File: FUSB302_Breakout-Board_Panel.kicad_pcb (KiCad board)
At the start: 2 copper layers, 100 x 100 mm, 75 parts, among them J1 Conn_01x07_Male, J2 Conn_01x07_Male, U1 FUSB302BMPX

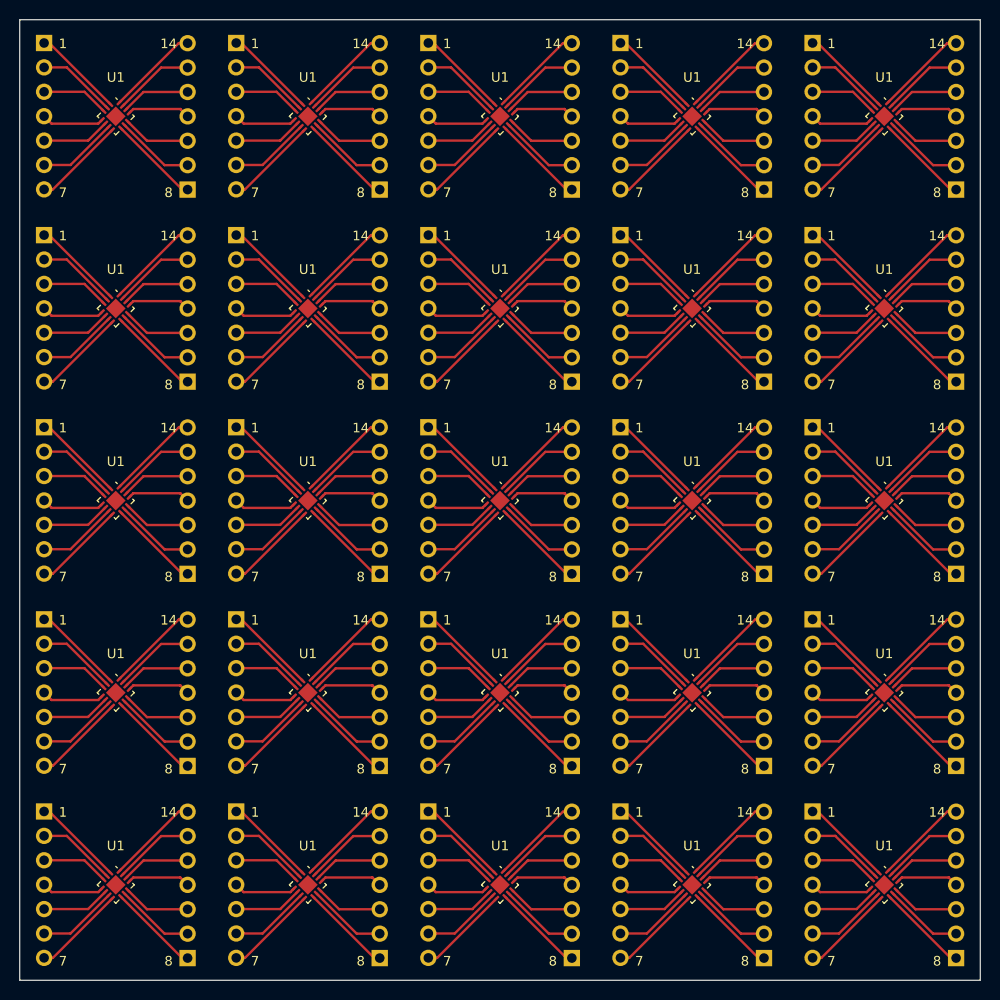
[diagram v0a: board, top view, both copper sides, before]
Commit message: Mod: PCB, added vias to filled zone on the bottom for a better heat path Mod: Panel, with new pcb Mod: Exports
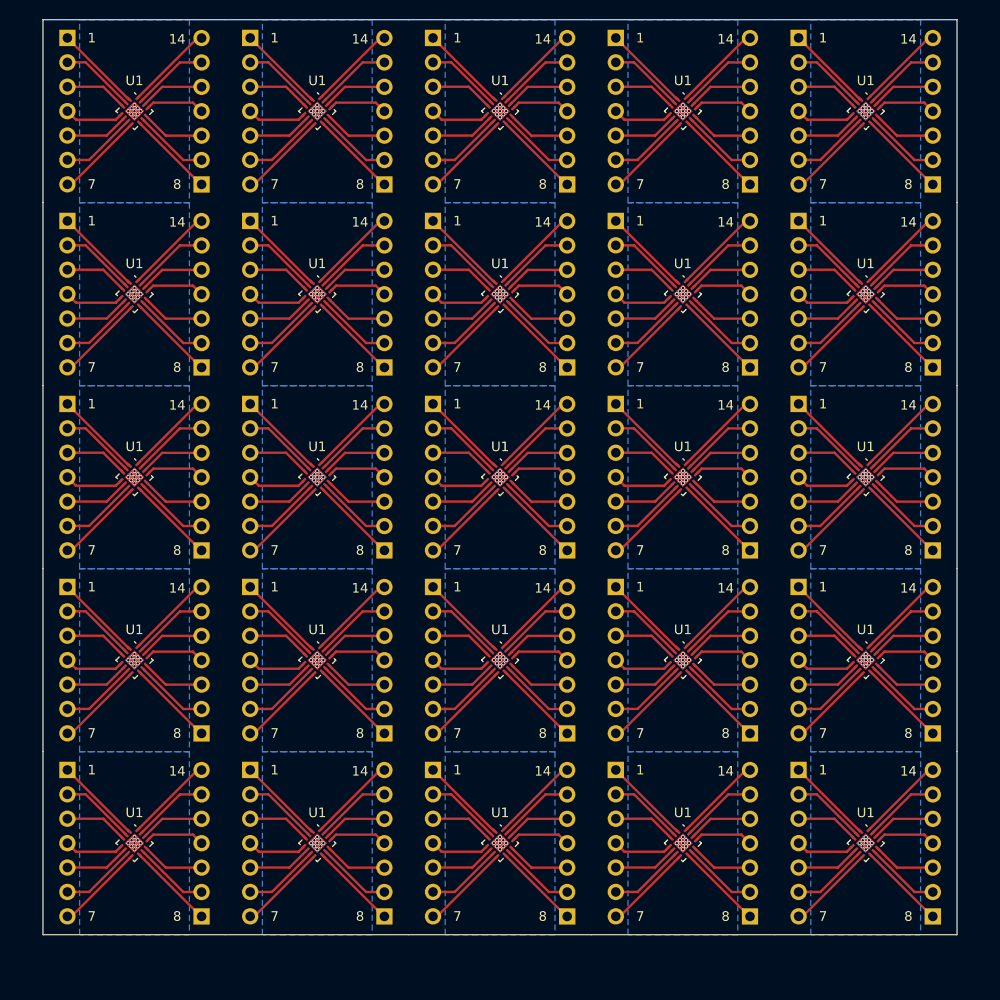
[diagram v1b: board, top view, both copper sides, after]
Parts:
- removed the J1 at (141.0, 92.4)
- removed the J1 at (101.0, 72.4)
- removed the J1 at (121.0, 72.4)
- removed the J1 at (121.0, 132.4)
- removed the J1 at (101.0, 112.4)
- removed the J1 at (141.0, 132.4)
- removed the J1 at (181.0, 92.4)
- removed the J1 at (181.0, 112.4)
- removed the J1 at (121.0, 92.4)
- removed the J1 at (141.0, 72.4)
- removed the J1 at (101.0, 132.4)
- removed the J1 at (181.0, 52.4)
- removed the J1 at (161.0, 92.4)
- removed the J1 at (181.0, 72.4)
- removed the J1 at (101.0, 92.4)
- removed the J1 at (181.0, 132.4)
- removed the J1 at (141.0, 52.4)
- removed the J1 at (161.0, 112.4)
- removed the J1 at (141.0, 112.4)
- removed the J1 at (121.0, 52.4)
- removed the J1 at (101.0, 52.4)
- removed the J1 at (121.0, 112.4)
- removed the J1 at (161.0, 72.4)
- removed the J1 at (161.0, 132.4)
- removed the J1 at (161.0, 52.4)
- removed the J2 at (156.0, 147.7)
- removed the J2 at (176.0, 107.7)
- removed the J2 at (116.0, 147.7)
- removed the J2 at (176.0, 67.7)
- removed the J2 at (116.0, 87.7)
- removed the J2 at (176.0, 87.7)
- removed the J2 at (136.0, 107.7)
- removed the J2 at (116.0, 127.7)
- removed the J2 at (196.0, 87.7)
- removed the J2 at (196.0, 147.7)
- removed the J2 at (136.0, 147.7)
- removed the J2 at (196.0, 127.7)
- removed the J2 at (176.0, 147.7)
- removed the J2 at (116.0, 107.7)
- removed the J2 at (196.0, 107.7)
- removed the J2 at (136.0, 87.7)
- removed the J2 at (196.0, 67.7)
- removed the J2 at (156.0, 127.7)
- removed the J2 at (136.0, 127.7)
- removed the J2 at (136.0, 67.7)
- removed the J2 at (116.0, 67.7)
- removed the J2 at (156.0, 67.7)
- removed the J2 at (176.0, 127.7)
- removed the J2 at (156.0, 87.7)
- removed the J2 at (156.0, 107.7)
- removed the U1 at (168.5, 120.1)
- removed the U1 at (168.5, 100.1)
- removed the U1 at (148.5, 100.1)
- removed the U1 at (168.5, 60.1)
- removed the U1 at (128.5, 120.1)
- removed the U1 at (108.5, 120.1)
- removed the U1 at (148.5, 80.1)
- removed the U1 at (188.5, 140.1)
- removed the U1 at (108.5, 100.1)
- removed the U1 at (188.5, 120.1)
- removed the U1 at (128.5, 140.1)
- removed the U1 at (108.5, 80.1)
- removed the U1 at (128.5, 60.1)
- removed the U1 at (108.5, 140.1)
- removed the U1 at (188.5, 60.1)
- removed the U1 at (168.5, 80.1)
- removed the U1 at (168.5, 140.1)
- removed the U1 at (148.5, 140.1)
- removed the U1 at (128.5, 80.1)
- removed the U1 at (148.5, 60.1)
- removed the U1 at (148.5, 120.1)
- removed the U1 at (128.5, 100.1)
- removed the U1 at (108.5, 60.1)
- removed the U1 at (188.5, 80.1)
- removed the U1 at (188.5, 100.1)
- added J1: Conn_01x07_Male, Connector_PinHeader_2.54mm:PinHeader_1x07_P2.54mm_Vertical, B.Cu at (160.6, 128.1)
- added J1: Conn_01x07_Male, Connector_PinHeader_2.54mm:PinHeader_1x07_P2.54mm_Vertical, B.Cu at (179.6, 51.9)
- added J1: Conn_01x07_Male, Connector_PinHeader_2.54mm:PinHeader_1x07_P2.54mm_Vertical, B.Cu at (141.5, 71.0)
- added J1: Conn_01x07_Male, Connector_PinHeader_2.54mm:PinHeader_1x07_P2.54mm_Vertical, B.Cu at (179.6, 109.0)
- added J1: Conn_01x07_Male, Connector_PinHeader_2.54mm:PinHeader_1x07_P2.54mm_Vertical, B.Cu at (103.5, 109.0)
- added J1: Conn_01x07_Male, Connector_PinHeader_2.54mm:PinHeader_1x07_P2.54mm_Vertical, B.Cu at (160.6, 71.0)
- added J1: Conn_01x07_Male, Connector_PinHeader_2.54mm:PinHeader_1x07_P2.54mm_Vertical, B.Cu at (103.5, 71.0)
- added J1: Conn_01x07_Male, Connector_PinHeader_2.54mm:PinHeader_1x07_P2.54mm_Vertical, B.Cu at (103.5, 90.0)
- added J1: Conn_01x07_Male, Connector_PinHeader_2.54mm:PinHeader_1x07_P2.54mm_Vertical, B.Cu at (179.6, 71.0)
- added J1: Conn_01x07_Male, Connector_PinHeader_2.54mm:PinHeader_1x07_P2.54mm_Vertical, B.Cu at (122.5, 109.0)
- added J1: Conn_01x07_Male, Connector_PinHeader_2.54mm:PinHeader_1x07_P2.54mm_Vertical, B.Cu at (179.6, 128.1)
- added J1: Conn_01x07_Male, Connector_PinHeader_2.54mm:PinHeader_1x07_P2.54mm_Vertical, B.Cu at (103.5, 51.9)
- added J1: Conn_01x07_Male, Connector_PinHeader_2.54mm:PinHeader_1x07_P2.54mm_Vertical, B.Cu at (160.6, 109.0)
- added J1: Conn_01x07_Male, Connector_PinHeader_2.54mm:PinHeader_1x07_P2.54mm_Vertical, B.Cu at (141.5, 109.0)
- added J1: Conn_01x07_Male, Connector_PinHeader_2.54mm:PinHeader_1x07_P2.54mm_Vertical, B.Cu at (141.5, 51.9)
- added J1: Conn_01x07_Male, Connector_PinHeader_2.54mm:PinHeader_1x07_P2.54mm_Vertical, B.Cu at (141.5, 90.0)
- added J1: Conn_01x07_Male, Connector_PinHeader_2.54mm:PinHeader_1x07_P2.54mm_Vertical, B.Cu at (122.5, 128.1)
- added J1: Conn_01x07_Male, Connector_PinHeader_2.54mm:PinHeader_1x07_P2.54mm_Vertical, B.Cu at (122.5, 71.0)
- added J1: Conn_01x07_Male, Connector_PinHeader_2.54mm:PinHeader_1x07_P2.54mm_Vertical, B.Cu at (179.6, 90.0)
- added J1: Conn_01x07_Male, Connector_PinHeader_2.54mm:PinHeader_1x07_P2.54mm_Vertical, B.Cu at (160.6, 90.0)
- added J1: Conn_01x07_Male, Connector_PinHeader_2.54mm:PinHeader_1x07_P2.54mm_Vertical, B.Cu at (141.5, 128.1)
- added J1: Conn_01x07_Male, Connector_PinHeader_2.54mm:PinHeader_1x07_P2.54mm_Vertical, B.Cu at (122.5, 51.9)
- added J1: Conn_01x07_Male, Connector_PinHeader_2.54mm:PinHeader_1x07_P2.54mm_Vertical, B.Cu at (160.6, 51.9)
- added J1: Conn_01x07_Male, Connector_PinHeader_2.54mm:PinHeader_1x07_P2.54mm_Vertical, B.Cu at (103.5, 128.1)
- added J1: Conn_01x07_Male, Connector_PinHeader_2.54mm:PinHeader_1x07_P2.54mm_Vertical, B.Cu at (122.5, 90.0)
- added J2: Conn_01x07_Male, Connector_PinHeader_2.54mm:PinHeader_1x07_P2.54mm_Vertical, B.Cu at (193.6, 124.3)
- added J2: Conn_01x07_Male, Connector_PinHeader_2.54mm:PinHeader_1x07_P2.54mm_Vertical, B.Cu at (155.5, 143.3)
- added J2: Conn_01x07_Male, Connector_PinHeader_2.54mm:PinHeader_1x07_P2.54mm_Vertical, B.Cu at (155.5, 124.3)
- added J2: Conn_01x07_Male, Connector_PinHeader_2.54mm:PinHeader_1x07_P2.54mm_Vertical, B.Cu at (136.5, 105.2)
- added J2: Conn_01x07_Male, Connector_PinHeader_2.54mm:PinHeader_1x07_P2.54mm_Vertical, B.Cu at (136.5, 124.3)
- added J2: Conn_01x07_Male, Connector_PinHeader_2.54mm:PinHeader_1x07_P2.54mm_Vertical, B.Cu at (155.5, 105.2)
- added J2: Conn_01x07_Male, Connector_PinHeader_2.54mm:PinHeader_1x07_P2.54mm_Vertical, B.Cu at (193.6, 105.2)
- added J2: Conn_01x07_Male, Connector_PinHeader_2.54mm:PinHeader_1x07_P2.54mm_Vertical, B.Cu at (193.6, 143.3)
- added J2: Conn_01x07_Male, Connector_PinHeader_2.54mm:PinHeader_1x07_P2.54mm_Vertical, B.Cu at (136.5, 143.3)
- added J2: Conn_01x07_Male, Connector_PinHeader_2.54mm:PinHeader_1x07_P2.54mm_Vertical, B.Cu at (174.5, 67.2)
- added J2: Conn_01x07_Male, Connector_PinHeader_2.54mm:PinHeader_1x07_P2.54mm_Vertical, B.Cu at (117.4, 105.2)
- added J2: Conn_01x07_Male, Connector_PinHeader_2.54mm:PinHeader_1x07_P2.54mm_Vertical, B.Cu at (174.5, 143.3)
- added J2: Conn_01x07_Male, Connector_PinHeader_2.54mm:PinHeader_1x07_P2.54mm_Vertical, B.Cu at (117.4, 124.3)
- added J2: Conn_01x07_Male, Connector_PinHeader_2.54mm:PinHeader_1x07_P2.54mm_Vertical, B.Cu at (117.4, 67.2)
- added J2: Conn_01x07_Male, Connector_PinHeader_2.54mm:PinHeader_1x07_P2.54mm_Vertical, B.Cu at (174.5, 86.2)
- added J2: Conn_01x07_Male, Connector_PinHeader_2.54mm:PinHeader_1x07_P2.54mm_Vertical, B.Cu at (117.4, 143.3)
- added J2: Conn_01x07_Male, Connector_PinHeader_2.54mm:PinHeader_1x07_P2.54mm_Vertical, B.Cu at (174.5, 124.3)
- added J2: Conn_01x07_Male, Connector_PinHeader_2.54mm:PinHeader_1x07_P2.54mm_Vertical, B.Cu at (155.5, 86.2)
- added J2: Conn_01x07_Male, Connector_PinHeader_2.54mm:PinHeader_1x07_P2.54mm_Vertical, B.Cu at (136.5, 67.2)
- added J2: Conn_01x07_Male, Connector_PinHeader_2.54mm:PinHeader_1x07_P2.54mm_Vertical, B.Cu at (193.6, 86.2)
- added J2: Conn_01x07_Male, Connector_PinHeader_2.54mm:PinHeader_1x07_P2.54mm_Vertical, B.Cu at (174.5, 105.2)
- added J2: Conn_01x07_Male, Connector_PinHeader_2.54mm:PinHeader_1x07_P2.54mm_Vertical, B.Cu at (193.6, 67.2)
- added J2: Conn_01x07_Male, Connector_PinHeader_2.54mm:PinHeader_1x07_P2.54mm_Vertical, B.Cu at (117.4, 86.2)
- added J2: Conn_01x07_Male, Connector_PinHeader_2.54mm:PinHeader_1x07_P2.54mm_Vertical, B.Cu at (136.5, 86.2)
- added J2: Conn_01x07_Male, Connector_PinHeader_2.54mm:PinHeader_1x07_P2.54mm_Vertical, B.Cu at (155.5, 67.2)
- added U1: FUSB302BMPX, Package_DFN_QFN:WQFN-14-1EP_2.5x2.5mm_P0.5mm_EP1.45x1.45mm, F.Cu at (110.5, 78.6)
- added U1: FUSB302BMPX, Package_DFN_QFN:WQFN-14-1EP_2.5x2.5mm_P0.5mm_EP1.45x1.45mm, F.Cu at (148.5, 116.7)
- added U1: FUSB302BMPX, Package_DFN_QFN:WQFN-14-1EP_2.5x2.5mm_P0.5mm_EP1.45x1.45mm, F.Cu at (110.5, 59.5)
- added U1: FUSB302BMPX, Package_DFN_QFN:WQFN-14-1EP_2.5x2.5mm_P0.5mm_EP1.45x1.45mm, F.Cu at (167.5, 78.6)
- added U1: FUSB302BMPX, Package_DFN_QFN:WQFN-14-1EP_2.5x2.5mm_P0.5mm_EP1.45x1.45mm, F.Cu at (167.5, 59.5)
- added U1: FUSB302BMPX, Package_DFN_QFN:WQFN-14-1EP_2.5x2.5mm_P0.5mm_EP1.45x1.45mm, F.Cu at (186.6, 116.7)
- added U1: FUSB302BMPX, Package_DFN_QFN:WQFN-14-1EP_2.5x2.5mm_P0.5mm_EP1.45x1.45mm, F.Cu at (148.5, 135.7)
- added U1: FUSB302BMPX, Package_DFN_QFN:WQFN-14-1EP_2.5x2.5mm_P0.5mm_EP1.45x1.45mm, F.Cu at (167.5, 97.6)
- added U1: FUSB302BMPX, Package_DFN_QFN:WQFN-14-1EP_2.5x2.5mm_P0.5mm_EP1.45x1.45mm, F.Cu at (186.6, 78.6)
- added U1: FUSB302BMPX, Package_DFN_QFN:WQFN-14-1EP_2.5x2.5mm_P0.5mm_EP1.45x1.45mm, F.Cu at (129.5, 59.5)
- added U1: FUSB302BMPX, Package_DFN_QFN:WQFN-14-1EP_2.5x2.5mm_P0.5mm_EP1.45x1.45mm, F.Cu at (129.5, 78.6)
- added U1: FUSB302BMPX, Package_DFN_QFN:WQFN-14-1EP_2.5x2.5mm_P0.5mm_EP1.45x1.45mm, F.Cu at (148.5, 59.5)
- added U1: FUSB302BMPX, Package_DFN_QFN:WQFN-14-1EP_2.5x2.5mm_P0.5mm_EP1.45x1.45mm, F.Cu at (186.6, 59.5)
- added U1: FUSB302BMPX, Package_DFN_QFN:WQFN-14-1EP_2.5x2.5mm_P0.5mm_EP1.45x1.45mm, F.Cu at (167.5, 116.7)
- added U1: FUSB302BMPX, Package_DFN_QFN:WQFN-14-1EP_2.5x2.5mm_P0.5mm_EP1.45x1.45mm, F.Cu at (167.5, 135.7)
- added U1: FUSB302BMPX, Package_DFN_QFN:WQFN-14-1EP_2.5x2.5mm_P0.5mm_EP1.45x1.45mm, F.Cu at (110.5, 116.7)
- added U1: FUSB302BMPX, Package_DFN_QFN:WQFN-14-1EP_2.5x2.5mm_P0.5mm_EP1.45x1.45mm, F.Cu at (186.6, 135.7)
- added U1: FUSB302BMPX, Package_DFN_QFN:WQFN-14-1EP_2.5x2.5mm_P0.5mm_EP1.45x1.45mm, F.Cu at (110.5, 135.7)
- added U1: FUSB302BMPX, Package_DFN_QFN:WQFN-14-1EP_2.5x2.5mm_P0.5mm_EP1.45x1.45mm, F.Cu at (148.5, 78.6)
- added U1: FUSB302BMPX, Package_DFN_QFN:WQFN-14-1EP_2.5x2.5mm_P0.5mm_EP1.45x1.45mm, F.Cu at (110.5, 97.6)
- added U1: FUSB302BMPX, Package_DFN_QFN:WQFN-14-1EP_2.5x2.5mm_P0.5mm_EP1.45x1.45mm, F.Cu at (148.5, 97.6)
- added U1: FUSB302BMPX, Package_DFN_QFN:WQFN-14-1EP_2.5x2.5mm_P0.5mm_EP1.45x1.45mm, F.Cu at (186.6, 97.6)
- added U1: FUSB302BMPX, Package_DFN_QFN:WQFN-14-1EP_2.5x2.5mm_P0.5mm_EP1.45x1.45mm, F.Cu at (129.5, 97.6)
- added U1: FUSB302BMPX, Package_DFN_QFN:WQFN-14-1EP_2.5x2.5mm_P0.5mm_EP1.45x1.45mm, F.Cu at (129.5, 135.7)
- added U1: FUSB302BMPX, Package_DFN_QFN:WQFN-14-1EP_2.5x2.5mm_P0.5mm_EP1.45x1.45mm, F.Cu at (129.5, 116.7)
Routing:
- net Board_0-VCONN: track 15.6 -> 14.6 mm
- net Board_5-VCONN: track 15.6 -> 14.6 mm
- net Board_20-VCONN: track 15.6 -> 14.6 mm
- net Board_19-GND: track 17.9 -> 16.9 mm, vias 0 -> 9
- net Board_18-GND: track 17.9 -> 16.9 mm, vias 0 -> 9
- net Board_17-GND: track 17.9 -> 16.9 mm, vias 0 -> 9
- net Board_16-GND: track 17.9 -> 16.9 mm, vias 0 -> 9
- net Board_14-GND: track 17.9 -> 16.9 mm, vias 0 -> 9
- net Board_13-GND: track 17.9 -> 16.9 mm, vias 0 -> 9
- net Board_12-GND: track 17.9 -> 16.9 mm, vias 0 -> 9
- net Board_11-GND: track 17.9 -> 16.9 mm, vias 0 -> 9
- net Board_9-GND: track 17.9 -> 16.9 mm, vias 0 -> 9
- net Board_8-GND: track 17.9 -> 16.9 mm, vias 0 -> 9
- net Board_7-GND: track 17.9 -> 16.9 mm, vias 0 -> 9
- net Board_6-GND: track 17.9 -> 16.9 mm, vias 0 -> 9
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- added copper zone on B.Cu, net Board_0-GND
- added copper zone on B.Cu, net Board_1-GND
- added copper zone on B.Cu, net Board_10-GND
- added copper zone on B.Cu, net Board_11-GND
- added copper zone on B.Cu, net Board_12-GND
- added copper zone on B.Cu, net Board_13-GND
- added copper zone on B.Cu, net Board_14-GND
- added copper zone on B.Cu, net Board_15-GND
- added copper zone on B.Cu, net Board_16-GND
- added copper zone on B.Cu, net Board_17-GND
- added copper zone on B.Cu, net Board_18-GND
- added copper zone on B.Cu, net Board_19-GND
- added copper zone on B.Cu, net Board_2-GND
- added copper zone on B.Cu, net Board_20-GND
- added copper zone on B.Cu, net Board_21-GND
- added copper zone on B.Cu, net Board_22-GND
- added copper zone on B.Cu, net Board_23-GND
- added copper zone on B.Cu, net Board_24-GND
- added copper zone on B.Cu, net Board_3-GND
- added copper zone on B.Cu, net Board_4-GND
- added copper zone on B.Cu, net Board_5-GND
- added copper zone on B.Cu, net Board_6-GND
- added copper zone on B.Cu, net Board_7-GND
- added copper zone on B.Cu, net Board_8-GND
- added copper zone on B.Cu, net Board_9-GND
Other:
- board size 100 x 100 mm -> 95.1 x 95.2 mm

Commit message: Mod: Bottom solder mask, pasted logo in to it and exported the pcb with the v-cuts
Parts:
- added G***: LOGO, drawings:elektronik-emblem_3x3.5_solder, B.Cu at (186.6, 130.0)
- added G***: LOGO, drawings:elektronik-emblem_3x3.5_solder, B.Cu at (110.5, 53.8)
- added G***: LOGO, drawings:elektronik-emblem_3x3.5_solder, B.Cu at (186.6, 53.8)
- added G***: LOGO, drawings:elektronik-emblem_3x3.5_solder, B.Cu at (167.5, 53.8)
- added G***: LOGO, drawings:elektronik-emblem_3x3.5_solder, B.Cu at (110.5, 111.0)
- added G***: LOGO, drawings:elektronik-emblem_3x3.5_solder, B.Cu at (148.5, 91.9)
- added G***: LOGO, drawings:elektronik-emblem_3x3.5_solder, B.Cu at (186.6, 111.0)
- added G***: LOGO, drawings:elektronik-emblem_3x3.5_solder, B.Cu at (129.5, 53.8)
- added G***: LOGO, drawings:elektronik-emblem_3x3.5_solder, B.Cu at (110.5, 91.9)
- added G***: LOGO, drawings:elektronik-emblem_3x3.5_solder, B.Cu at (167.5, 130.0)
- added G***: LOGO, drawings:elektronik-emblem_3x3.5_solder, B.Cu at (129.5, 130.0)
- added G***: LOGO, drawings:elektronik-emblem_3x3.5_solder, B.Cu at (129.5, 111.0)
- added G***: LOGO, drawings:elektronik-emblem_3x3.5_solder, B.Cu at (186.6, 72.9)
- added G***: LOGO, drawings:elektronik-emblem_3x3.5_solder, B.Cu at (129.5, 72.9)
- added G***: LOGO, drawings:elektronik-emblem_3x3.5_solder, B.Cu at (167.5, 72.9)
- added G***: LOGO, drawings:elektronik-emblem_3x3.5_solder, B.Cu at (110.5, 72.9)
- added G***: LOGO, drawings:elektronik-emblem_3x3.5_solder, B.Cu at (110.5, 130.0)
- added G***: LOGO, drawings:elektronik-emblem_3x3.5_solder, B.Cu at (167.5, 111.0)
- added G***: LOGO, drawings:elektronik-emblem_3x3.5_solder, B.Cu at (148.5, 130.0)
- added G***: LOGO, drawings:elektronik-emblem_3x3.5_solder, B.Cu at (148.5, 111.0)
- added G***: LOGO, drawings:elektronik-emblem_3x3.5_solder, B.Cu at (148.5, 53.8)
- added G***: LOGO, drawings:elektronik-emblem_3x3.5_solder, B.Cu at (129.5, 91.9)
- added G***: LOGO, drawings:elektronik-emblem_3x3.5_solder, B.Cu at (148.5, 72.9)
- added G***: LOGO, drawings:elektronik-emblem_3x3.5_solder, B.Cu at (186.6, 91.9)
- added G***: LOGO, drawings:elektronik-emblem_3x3.5_solder, B.Cu at (167.5, 91.9)

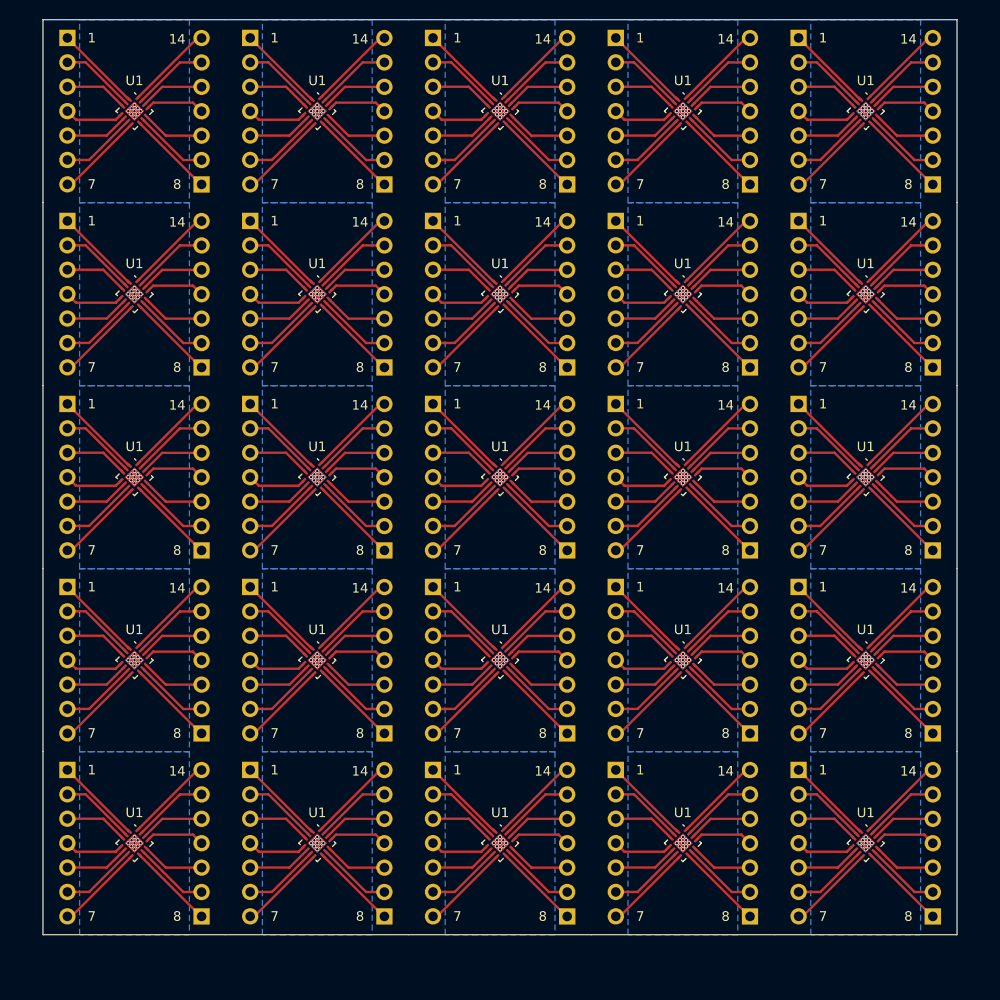
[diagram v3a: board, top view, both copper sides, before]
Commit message: Mod: Corrected trace to first pin, added Rev. and Prj. to the bottom solder mask
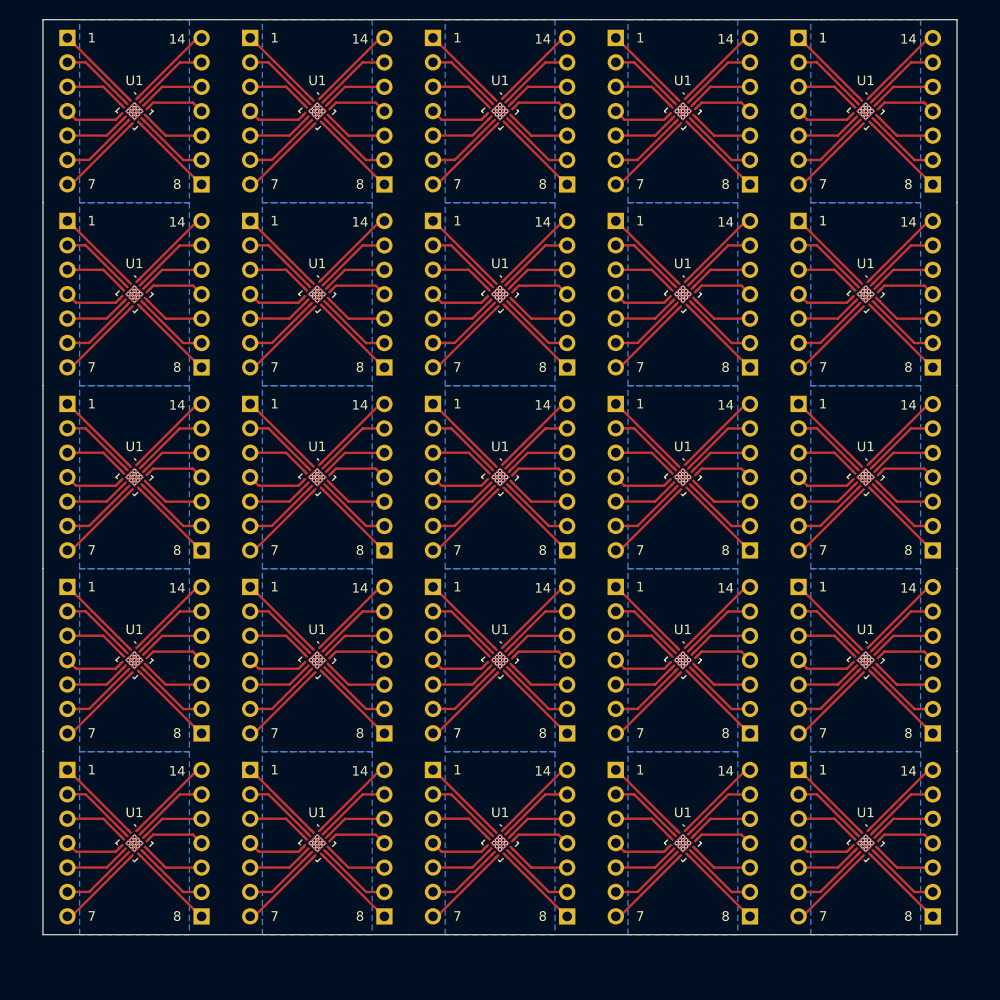
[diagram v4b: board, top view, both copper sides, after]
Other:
- board text added: "Prj: ${TITLE} Rev: ${REVISION}"

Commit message: Mod: Updated the project name and revision to be on the copper layer now
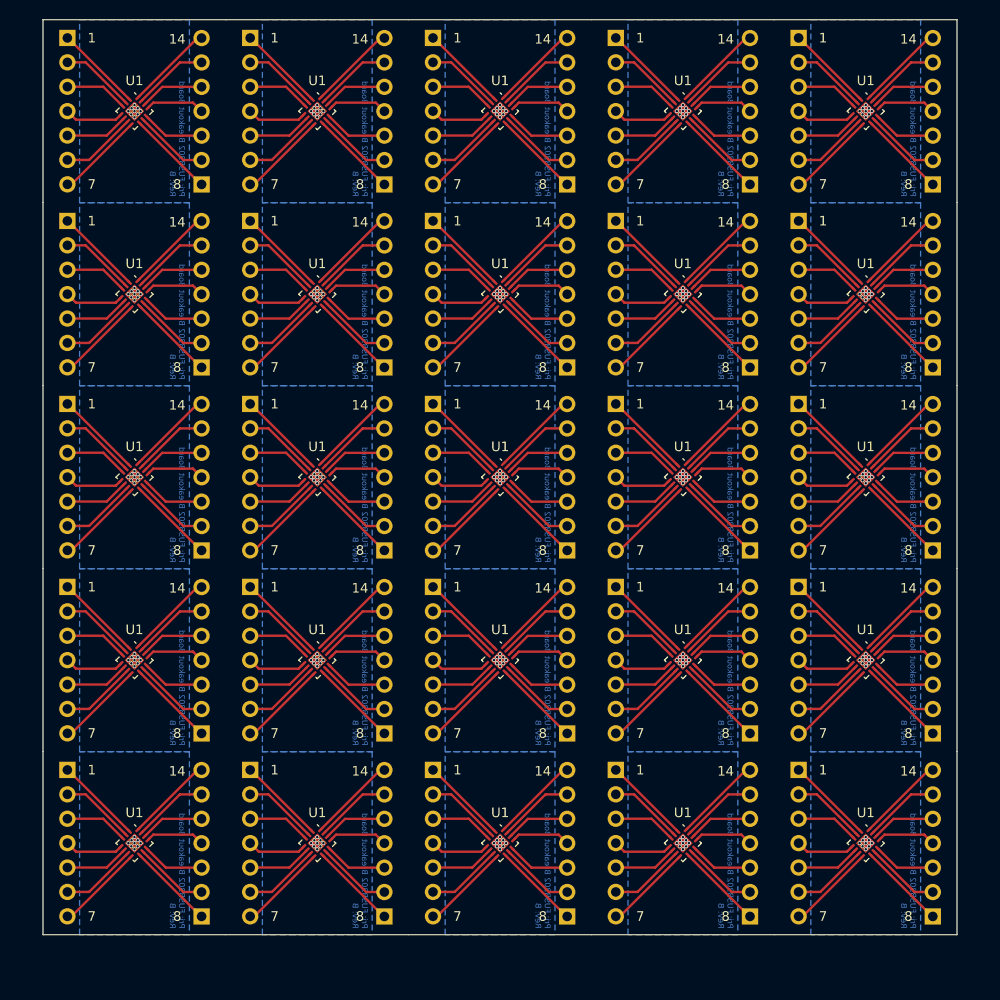
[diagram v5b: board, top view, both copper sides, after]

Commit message: Mod: The project name string
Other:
- board text added: "${TITLE} Rev: ${REVISION}"
- board text removed: "Prj: ${TITLE} Rev: ${REVISION}"
